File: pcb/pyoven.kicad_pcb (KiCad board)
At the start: 2 copper layers, 160 x 57 mm, 92 parts, among them J1 USB_C_Receptacle, J10 Conn_01x01, J11 Conn_01x01, J12 Conn_01x01, J13 Conn_01x01, J14 Conn_01x01, J15 Conn_01x01, J16 Conn_01x01, J17 Conn_01x01, J18 Conn_01x01, J19 Conn_02x05_Odd_Even, J2 Conn_01x12, J3 Conn_01x08, J4 Conn_01x01, J5 Conn_01x01, J6 Conn_01x01, J7 Conn_01x01, J8 Conn_01x01, J9 Conn_01x01, Q1 BSS138, Q2 BSS138, SW1 Frozen, SW2 More, SW3 Start, SW4 C/F, SW5 Dec, SW6 Temp, SW7 Time, SW8 Inc, SW9 Reset, U1 PCF8551ATT, U2 SAMD51J, U3 L7805, U4 AP2204K-1.5

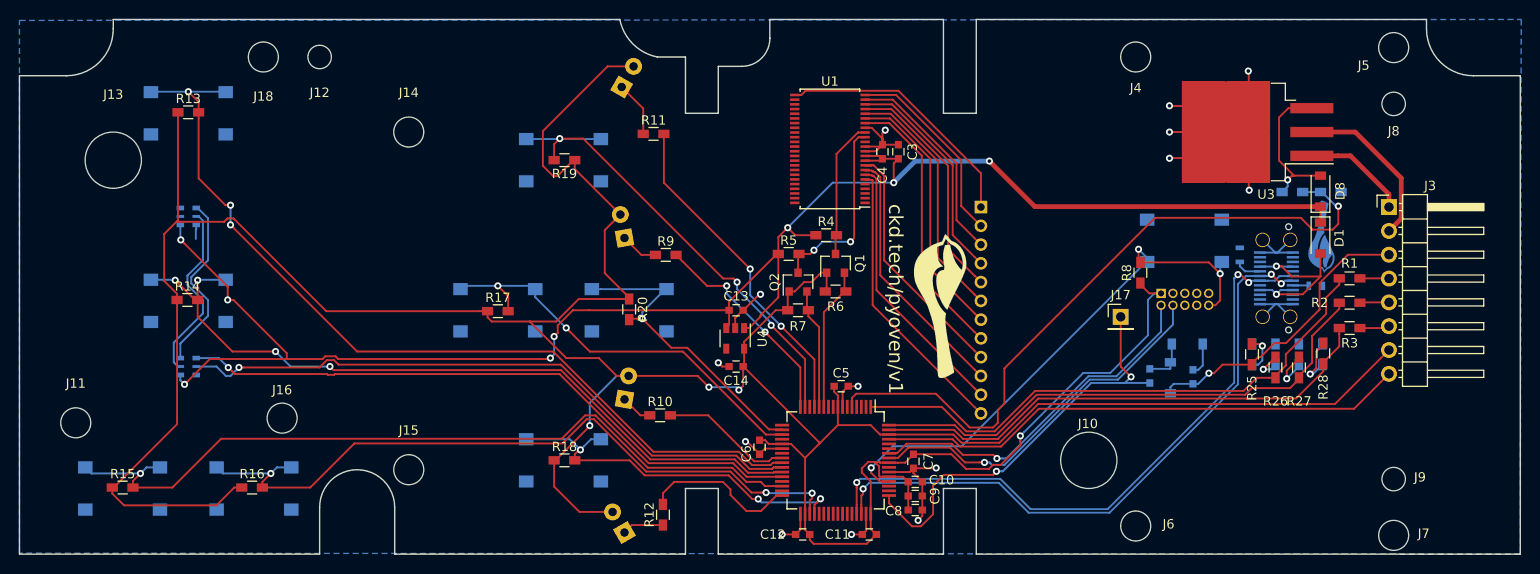
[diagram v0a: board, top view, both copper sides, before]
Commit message: A number of fixes: * lcd pin swap * button location tweak * temp divider resistor * correct regulator footprint
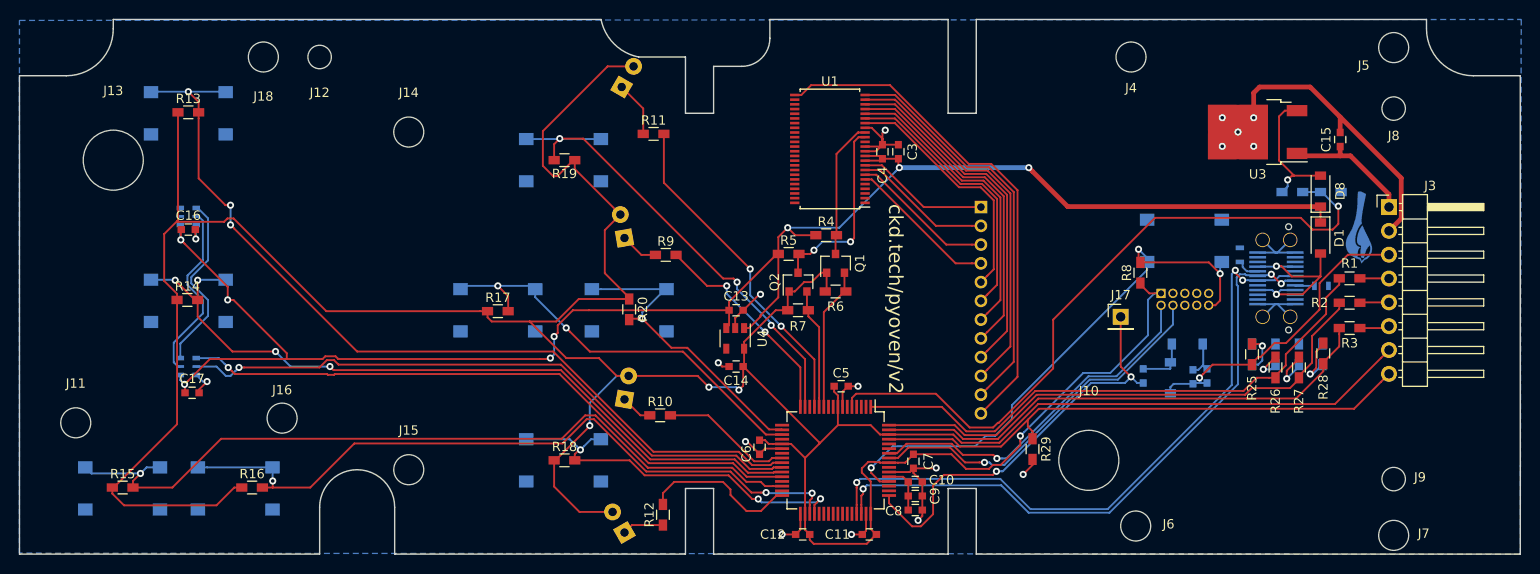
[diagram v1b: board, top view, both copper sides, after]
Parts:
- removed the G*** at (198.0, 73.8)
- added C15: 1uF, Capacitors_SMD:C_0603, F.Cu at (240.8, 55.8)
- added C16: 0.1uF, Capacitors_SMD:C_0603, F.Cu at (118.0, 65.4)
- added C17: 0.1uF, Capacitors_SMD:C_0603, F.Cu at (118.4, 82.8)
- added C18: 10uF, Capacitors_SMD:C_0603, B.Cu at (226.6, 81.0)
- added R29: 10k, Resistors_SMD:R_0603_HandSoldering, F.Cu at (208.0, 88.8)
- J1: footprint jae:DX07S024WJ3-OSHPARK -> jae:DX07S024WJ3-OSHPARK-HS
- J10, J13: footprint Mounting_Holes:MountingHole_6mm -> Mounting_Holes:MountingHole_6.4mm_M6
- R1, R2, R3: value 5.1k -> 3.3k
- U3: footprint TO_SOT_Packages_SMD:TO-263-3_TabPin2 -> TO_SOT_Packages_SMD:TO-252-2
- moved G*** 4.12 mm to (242.8, 65.2)
- moved SW4 2.00 mm to (123.0, 93.0)
- moved C1 0.70 mm to (219.8, 81.0)
- moved R22 0.60 mm to (238.8, 71.4)
- moved J4 0.50 mm to (218.5, 47.0)
- moved J8 0.50 mm to (246.5, 52.5)
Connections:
- C10 pad 1: +3V3 -> Net-(C10-Pad1)
- C8 pad 1: +3V3 -> Net-(C10-Pad1)
- C9 pad 1: +3V3 -> Net-(C10-Pad1)
- J2 pad 1: /SEG7 -> /COM3
- J2 pad 10: /COM2 -> /SEG5
- J2 pad 11: /COM1 -> /SEG6
- J2 pad 12: /COM0 -> /SEG7
- J2 pad 2: /SEG6 -> /COM2
- J2 pad 3: /SEG5 -> /COM1
- J2 pad 4: /SEG4 -> /COM0
- J2 pad 5: /SEG3 -> /SEG0
- J2 pad 6: /SEG2 -> /SEG1
- J2 pad 7: /SEG1 -> /SEG2
- J2 pad 8: /SEG0 -> /SEG3
- J2 pad 9: /COM3 -> /SEG4
- U2 pad 53: +3V3 -> Net-(C10-Pad1)
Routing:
- net /SEG7: track 27.3 -> 54.2 mm
- net /SEG6: track 21.0 -> 43.2 mm
- net /SEG5: track 22.3 -> 40.4 mm
- net /COM0: track 30.5 -> 16.1 mm
- net /SEG4: track 23.7 -> 37.6 mm
- net /COM1: track 29.0 -> 15.4 mm
- net /COM3: track 27.5 -> 14.2 mm
- net /COM2: track 27.6 -> 14.8 mm
- net /SEG3: track 25.2 -> 34.8 mm
- net +3V3: track 391.4 -> 383.4 mm
- net GNDPWR: track 101.9 -> 109.8 mm, vias 14 -> 17
- net /SEG2: track 26.7 -> 32.0 mm
- net Net-(C10-Pad1): track 0.00 -> 5.28 mm
- net /SEG0: track 29.6 -> 26.4 mm
- net +VDC: track 11.3 -> 14.0 mm
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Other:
- outline, holes or cut-outs redrawn
- board text added: "ckd.tech/pyoven/v2"
- board text added: "pyoven 2.0.0"
- board text removed: "ckd.tech/pyoven/v1"
- board text removed: "pyoven 1.0.0"
